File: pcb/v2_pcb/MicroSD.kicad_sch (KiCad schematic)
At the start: 7 parts, among them J3 DM3CS-SF

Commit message: add rpls for 1v8, 5v
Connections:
- net +3V3 renamed +3V3_MAIN
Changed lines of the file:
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@@
 			)
 		)
-		(property "Value" "+3V3"
+		(property "Value" "+3V3_MAIN"
 			(at 133.35 100.3299 90)
 			(show_name no)
@@
 			)
 		)
-		(property "Value" "+3V3"
+		(property "Value" "+3V3_MAIN"
 			(at 204.47 115.5699 90)
 			(show_name no)
@@
 			)
 		)
-		(property "Value" "+3V3"
+		(property "Value" "+3V3_MAIN"
 			(at 128.27 85.0899 90)
 			(show_name no)

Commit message: pcb done
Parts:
- added C306: 100nF, Capacitor_SMD:C_0402_1005Metric, symbol Device:C_Small
- added C307: 10uF, Capacitor_SMD:C_0805_2012Metric, symbol Device:C_Small
- J3: footprint DM3CS-SF_HIR -> noob:DM3CS-SF_HIR; MPN (none) -> DM3CS-SF; Manufacturer (none) -> Hirose
- R14, R15, R16, R17, R18, R19: footprint (none) -> Resistor_SMD:R_0402_1005Metric
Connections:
- net +3V3_MAIN: now also R14.1, R15.1, R16.1, C306.1, C307.1; no longer R14.2, R15.2, R16.2
- net GND: now also C306.2, C307.2
- net SDMMC_CDS renamed SD_CD_N
- net SD_CD_N: now also R19.2; no longer R14.1
- net SDMMC_CK renamed SD_CLK
- net SDMMC_CMD renamed SD_CMD
- net SD_CMD: now also R18.2; no longer R17.2
- net SDMMC_D0 renamed SD_D0
- net SD_D0: now also R14.2; no longer R16.1
- net SDMMC_D1 renamed SD_D1
- net SD_D1: now also R15.2; no longer R15.1
- net SDMMC_D2 renamed SD_D2
- net SD_D2: now also R16.2; no longer R19.2
- net SDMMC_D3 renamed SD_D3
- net SD_D3: now also R17.2; no longer R18.2
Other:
- moved on the sheet: J3

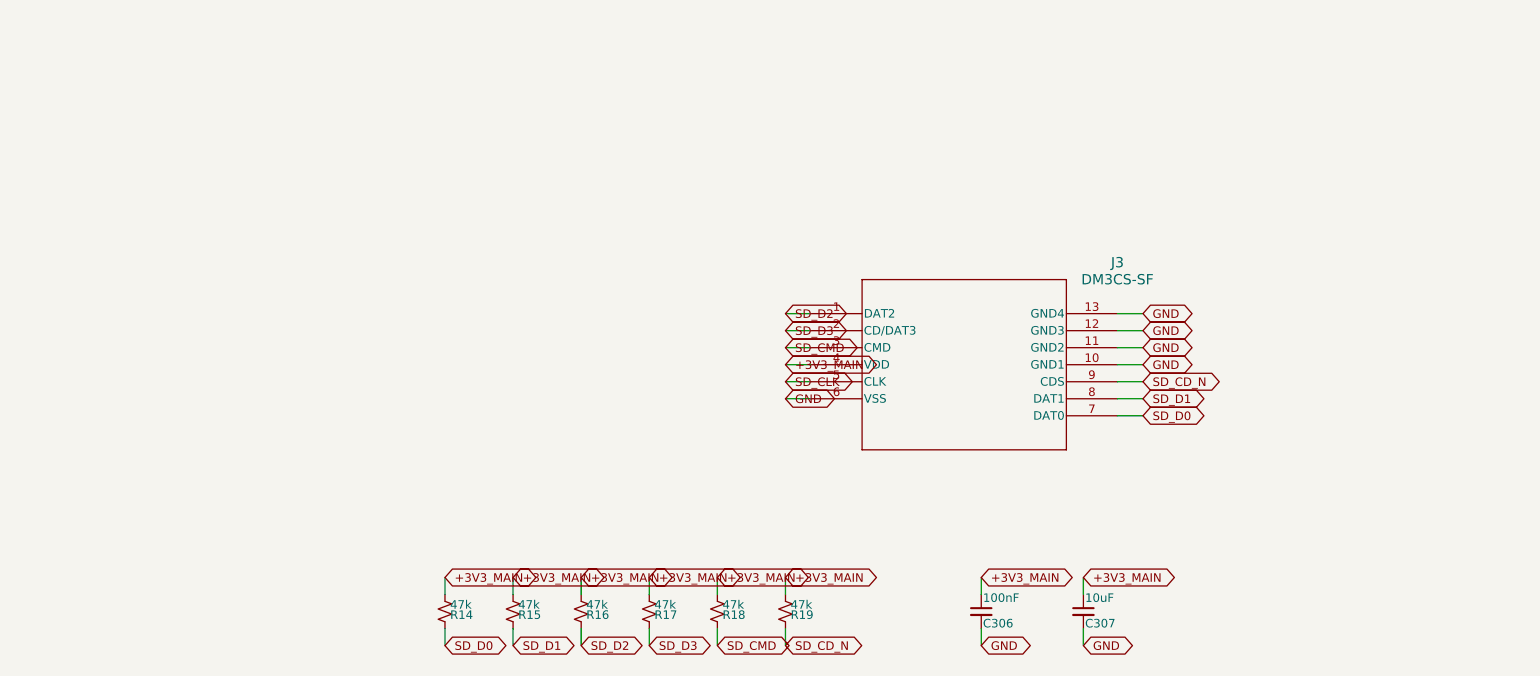
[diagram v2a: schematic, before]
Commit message: switch mosfets
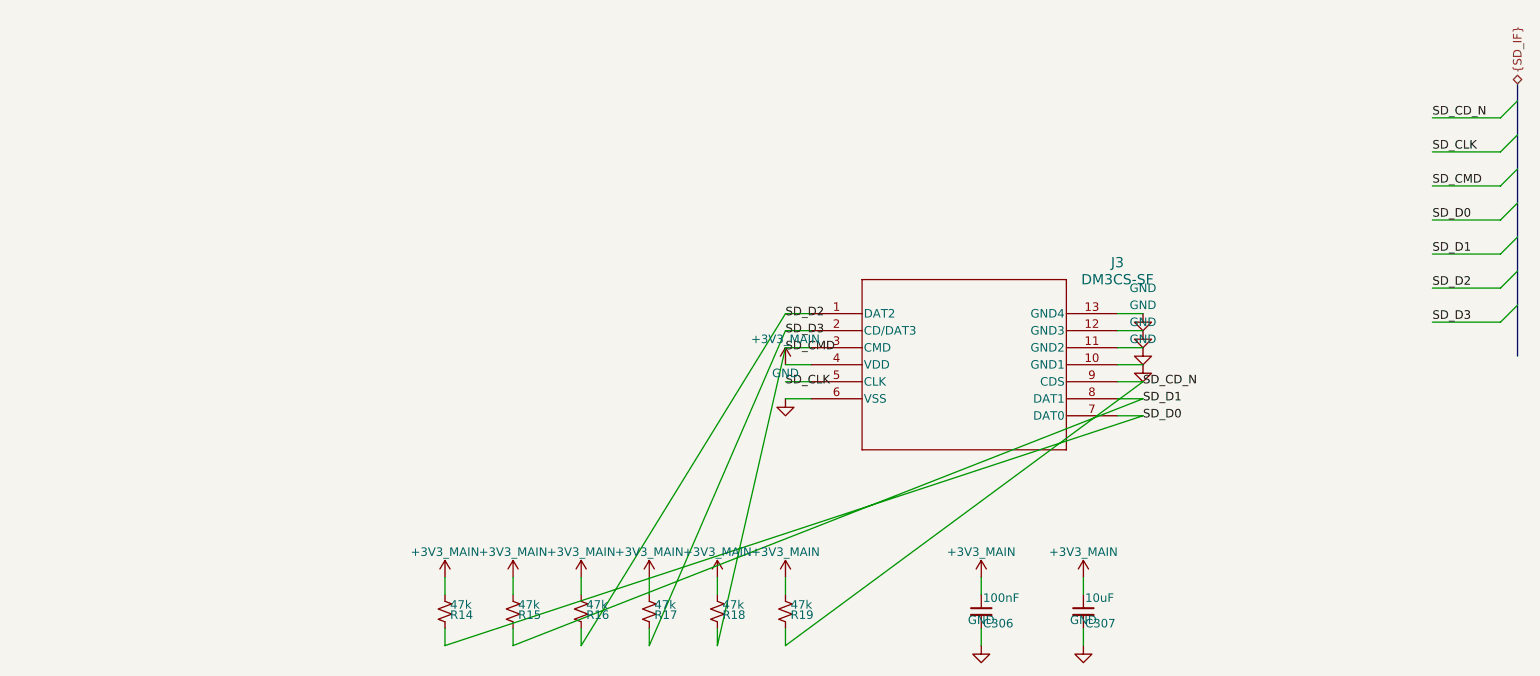
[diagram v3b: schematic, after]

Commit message: clean pcb
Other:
- moved on the sheet: C306, C307, R14, R15, R16, R17, R18, R19

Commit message: minor fixes
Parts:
- C306: value 100nF -> 100nF 50V X7R; Dielectric (none) -> X7R; MPN (none) -> CGA2B3X7R1H104K050BE; Manufacturer (none) -> TDK; Qualification (none) -> AEC-Q200; Termination (none) -> Soft termination; Tolerance (none) -> ±10%; Voltage (none) -> 50 VDC
- C307: value 10uF -> 10uF 10V X7R; Dielectric (none) -> X7R; MPN (none) -> GCJ21BR71A106KE01L; Manufacturer (none) -> Murata; Qualification (none) -> AEC-Q200; Termination (none) -> Soft termination; Tolerance (none) -> ±10%; Voltage (none) -> 10 VDC
- R14, R15, R16, R17, R18, R19: MPN (none) -> CRCW040247K0FKED; Manufacturer (none) -> Vishay; Power (none) -> 0.063 W; TCR (none) -> ±100 ppm/K; Tolerance (none) -> ±1%
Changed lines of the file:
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@@
 			)
 		)
-		(property "Datasheet" ""
+		(property "Datasheet" "https://www.vishay.com/docs/20035/dcrcwe3.pdf"
 			(at 109.22 83.82 0)
 			(show_name no)
@@
 			)
 		)
+    (property "Manufacturer" "Vishay" (at 109.22 83.82 0)
+      (effects (font (size 1.27 1.27)) (hide yes))
+    )
+    (property "MPN" "CRCW040247K0FKED" (at 109.22 83.82 0)
+      (effects (font (size 1.27 1.27)) (hide yes))
+    )
+    (property "Tolerance" "±1%" (at 109.22 83.82 0)
+      (effects (font (size 1.27 1.27)) (hide yes))
+    )
+    (property "Power" "0.063 W" (at 109.22 83.82 0)
+      (effects (font (size 1.27 1.27)) (hide yes))
+    )
+    (property "TCR" "±100 ppm/K" (at 109.22 83.82 0)
+      (effects (font (size 1.27 1.27)) (hide yes))
+    )
 		(pin "1"
 		)
@@
 			)
 		)
-		(property "Datasheet" "DM3CS-SF"
+		(property "Datasheet" "https://www.hirose.com/product/download/?distributor=all&lang=en&num=DM3CS-SF&type=specSheet"
 			(at 142.24 92.71 0)
 			(hide yes)
@@
 			)
 		)
-		(property "Description" ""
+		(property "Description" "Hirose DM3CS-SF hinged push-pull microSD socket"
 			(at 142.24 92.71 0)
 			(hide yes)
@@
 			)
 		)
-		(property "Value" "100nF"
+		(property "Value" "100nF 50V X7R"
 			(at 97.536 113.792 0)
 			(show_name no)
@@
 			)
 		)
-		(property "Datasheet" ""
+		(property "Datasheet" "https://product.tdk.com/en/search/capacitor/ceramic/mlcc/info?part_no=CGA2B3X7R1H104K050BE"
 			(at 104.14 111.76 0)
 			(show_name no)
@@
 			)
 		)
+    (property "Manufacturer" "TDK" (at 104.14 111.76 0)
+      (effects (font (size 1.27 1.27)) (hide yes))
+    )
+    (property "MPN" "CGA2B3X7R1H104K050BE" (at 104.14 111.76 0)
+      (effects (font (size 1.27 1.27)) (hide yes))
+    )
+    (property "Voltage" "50 VDC" (at 104.14 111.76 0)
+      (effects (font (size 1.27 1.27)) (hide yes))
+    )
+    (property "Tolerance" "±10%" (at 104.14 111.76 0)
+      (effects (font (size 1.27 1.27)) (hide yes))
+    )
+    (property "Dielectric" "X7R" (at 104.14 111.76 0)
+      (effects (font (size 1.27 1.27)) (hide yes))
+    )
+    (property "Qualification" "AEC-Q200" (at 104.14 111.76 0)
+      (effects (font (size 1.27 1.27)) (hide yes))
+    )
+    (property "Termination" "Soft termination" (at 104.14 111.76 0)
+      (effects (font (size 1.27 1.27)) (hide yes))
+    )
 		(pin "1"
 		)
@@
 			)
 		)
-		(property "Datasheet" ""
+		(property "Datasheet" "https://www.vishay.com/docs/20035/dcrcwe3.pdf"
 			(at 180.34 83.82 0)
 			(show_name no)
@@
 			)
 		)
+    (property "Manufacturer" "Vishay" (at 180.34 83.82 0)
+      (effects (font (size 1.27 1.27)) (hide yes))
+    )
+    (property "MPN" "CRCW040247K0FKED" (at 180.34 83.82 0)
+      (effects (font (size 1.27 1.27)) (hide yes))
+    )
+    (property "Tolerance" "±1%" (at 180.34 83.82 0)
+      (effects (font (size 1.27 1.27)) (hide yes))
+    )
+    (property "Power" "0.063 W" (at 180.34 83.82 0)
+      (effects (font (size 1.27 1.27)) (hide yes))
+    )
+    (property "TCR" "±100 ppm/K" (at 180.34 83.82 0)
+      (effects (font (size 1.27 1.27)) (hide yes))
+    )
 		(pin "1"
 		)
@@
 			)
 		)
-		(property "Datasheet" ""
+		(property "Datasheet" "https://www.vishay.com/docs/20035/dcrcwe3.pdf"
 			(at 104.14 83.82 0)
 			(show_name no)
@@
 			)
 		)
+    (property "Manufacturer" "Vishay" (at 104.14 83.82 0)
+      (effects (font (size 1.27 1.27)) (hide yes))
+    )
+    (property "MPN" "CRCW040247K0FKED" (at 104.14 83.82 0)
+      (effects (font (size 1.27 1.27)) (hide yes))
+    )
+    (property "Tolerance" "±1%" (at 104.14 83.82 0)
+      (effects (font (size 1.27 1.27)) (hide yes))
+    )
+    (property "Power" "0.063 W" (at 104.14 83.82 0)
+      (effects (font (size 1.27 1.27)) (hide yes))
+    )
+    (property "TCR" "±100 ppm/K" (at 104.14 83.82 0)
+      (effects (font (size 1.27 1.27)) (hide yes))
+    )
 		(pin "1"
 		)
@@
 			)
 		)
-		(property "Datasheet" ""
+		(property "Datasheet" "https://www.vishay.com/docs/20035/dcrcwe3.pdf"
 			(at 190.5 83.82 0)
 			(show_name no)
@@
 			)
 		)
+    (property "Manufacturer" "Vishay" (at 190.5 83.82 0)
+      (effects (font (size 1.27 1.27)) (hide yes))
+    )
+    (property "MPN" "CRCW040247K0FKED" (at 190.5 83.82 0)
+      (effects (font (size 1.27 1.27)) (hide yes))
+    )
+    (property "Tolerance" "±1%" (at 190.5 83.82 0)
+      (effects (font (size 1.27 1.27)) (hide yes))
+    )
+    (property "Power" "0.063 W" (at 190.5 83.82 0)
+      (effects (font (size 1.27 1.27)) (hide yes))
+    )
+    (property "TCR" "±100 ppm/K" (at 190.5 83.82 0)
+      (effects (font (size 1.27 1.27)) (hide yes))
+    )
 		(pin "1"
 		)
@@
 			)
 		)
-		(property "Datasheet" ""
+		(property "Datasheet" "https://www.vishay.com/docs/20035/dcrcwe3.pdf"
 			(at 99.06 83.82 0)
 			(show_name no)
@@
 			)
 		)
+    (property "Manufacturer" "Vishay" (at 99.06 83.82 0)
+      (effects (font (size 1.27 1.27)) (hide yes))
+    )
+    (property "MPN" "CRCW040247K0FKED" (at 99.06 83.82 0)
+      (effects (font (size 1.27 1.27)) (hide yes))
+    )
+    (property "Tolerance" "±1%" (at 99.06 83.82 0)
+      (effects (font (size 1.27 1.27)) (hide yes))
+    )
+    (property "Power" "0.063 W" (at 99.06 83.82 0)
+      (effects (font (size 1.27 1.27)) (hide yes))
+    )
+    (property "TCR" "±100 ppm/K" (at 99.06 83.82 0)
+      (effects (font (size 1.27 1.27)) (hide yes))
+    )
 		(pin "1"
 		)
@@
 			)
 		)
-		(property "Datasheet" ""
+		(property "Datasheet" "https://www.vishay.com/docs/20035/dcrcwe3.pdf"
 			(at 185.42 83.82 0)
 			(show_name no)
@@
 			)
 		)
+    (property "Manufacturer" "Vishay" (at 185.42 83.82 0)
+      (effects (font (size 1.27 1.27)) (hide yes))
+    )
+    (property "MPN" "CRCW040247K0FKED" (at 185.42 83.82 0)
+      (effects (font (size 1.27 1.27)) (hide yes))
+    )
+    (property "Tolerance" "±1%" (at 185.42 83.82 0)
+      (effects (font (size 1.27 1.27)) (hide yes))
+    )
+    (property "Power" "0.063 W" (at 185.42 83.82 0)
+      (effects (font (size 1.27 1.27)) (hide yes))
+    )
+    (property "TCR" "±100 ppm/K" (at 185.42 83.82 0)
+      (effects (font (size 1.27 1.27)) (hide yes))
+    )
 		(pin "1"
 		)
@@
 			)
 		)
-		(property "Value" "10uF"
+		(property "Value" "10uF 10V X7R"
 			(at 110.744 113.792 0)
 			(show_name no)
@@
 			)
 		)
-		(property "Datasheet" ""
+		(property "Datasheet" "https://www.murata.com/en-global/products/productdetail?partno=GCJ21BR71A106KE01%23"
 			(at 109.22 111.76 0)
 			(show_name no)
@@
 			)
 		)
-		(pin "1"
-		)
+    (property "Manufacturer" "Murata" (at 109.22 111.76 0)
+      (effects (font (size 1.27 1.27)) (hide yes))
+    )
+    (property "MPN" "GCJ21BR71A106KE01L" (at 109.22 111.76 0)
+      (effects (font (size 1.27 1.27)) (hide yes))
+    )
+    (property "Voltage" "10 VDC" (at 109.22 111.76 0)
+      (effects (font (size 1.27 1.27)) (hide yes))
+    )
+    (property "Tolerance" "±10%" (at 109.22 111.76 0)
+      (effects (font (size 1.27 1.27)) (hide yes))
+    )
+    (property "Dielectric" "X7R" (at 109.22 111.76 0)
+      (effects (font (size 1.27 1.27)) (hide yes))
+    )
+    (property "Termination" "Soft termination" (at 109.22 111.76 0)
+      (effects (font (size 1.27 1.27)) (hide yes))
+    )
+    (property "Qualification" "AEC-Q200" (at 109.22 111.76 0)
+      (effects (font (size 1.27 1.27)) (hide yes))
+    )
+		(pin "1"
+		)
